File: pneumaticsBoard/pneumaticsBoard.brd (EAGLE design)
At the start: 188 x 25.4 mm, 52 parts, among them IC1 MAX232, Q1 BSS296, Q2 BSS296, Q3 BSS296, Q4 BSS296, Q5 BSS296, Q6 BSS296, Q7 BSS296, Q8 BSS296, U1 ATMEGA328P-PU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

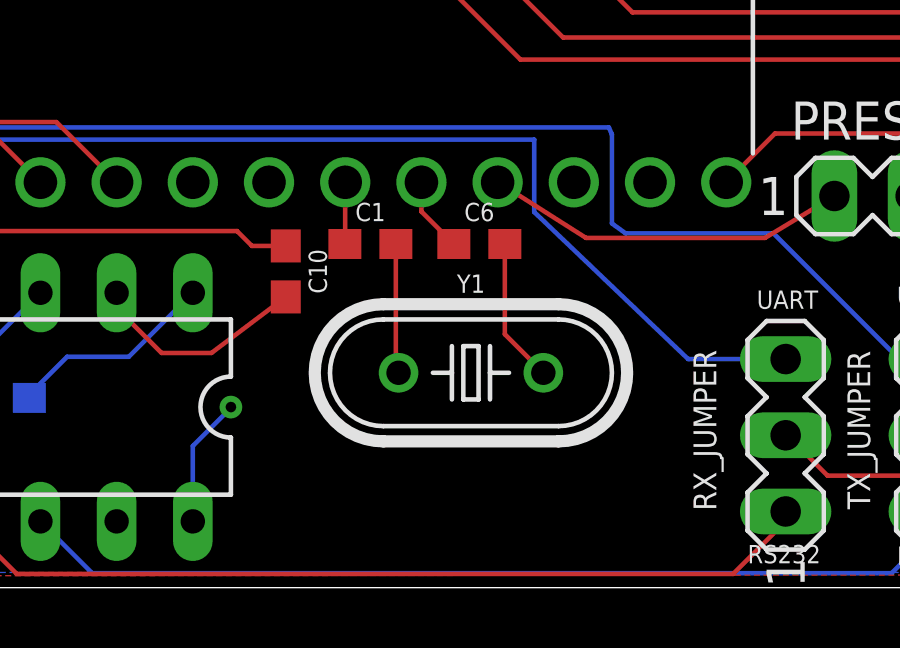
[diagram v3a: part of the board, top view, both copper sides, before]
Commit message: Crystal Circuit wasn't grounded
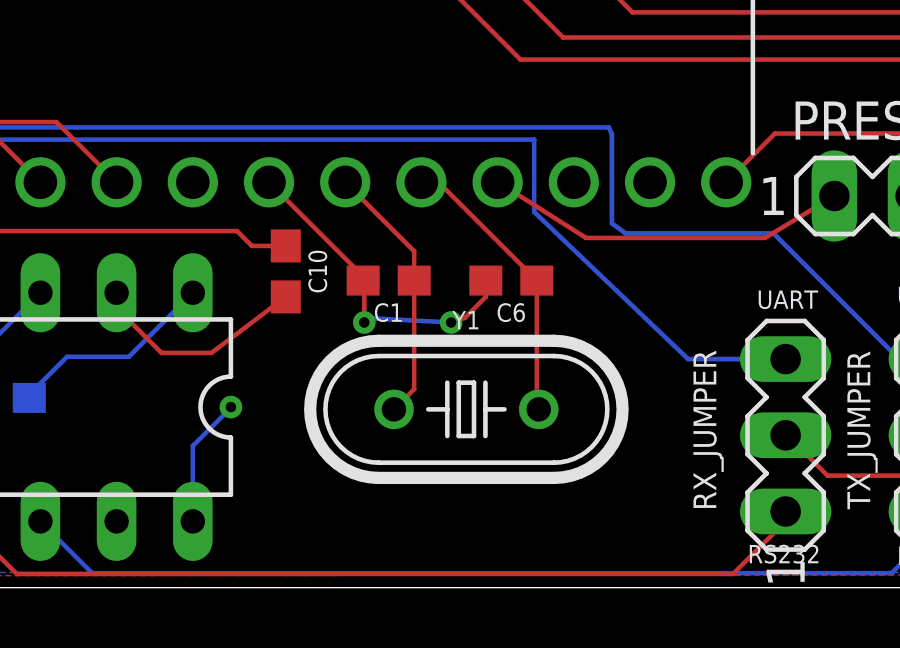
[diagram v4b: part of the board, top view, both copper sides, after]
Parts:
- moved C6 1.62 mm to (48.6, 10.2), turned to 180 degrees
- moved C1 1.36 mm to (44.6, 10.2), turned to 180 degrees
- moved Y1 1.23 mm to (47.1, 5.94)
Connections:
- removed net N$15: C1.2, Y1.1
- removed net N$5: C6.2, Y1.2
- net GND: now also C1.2, C6.2
- net XTAL1: now also Y1.1
- net XTAL2: now also Y1.2
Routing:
- net GND: track 33.7 -> 44.8 mm, vias 0 -> 2
- net XTAL2: track 2.50 -> 9.52 mm
- net XTAL1: track 2.06 -> 8.80 mm
- net N$5: track 4.82 -> 0.00 mm
- net N$15: track 4.33 -> 0.00 mm
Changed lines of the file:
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@@
 <attribute name="SUPPLIER" value="Atmel" x="55.8038" y="21.1328" size="1.778" layer="27" rot="R90" display="off"/>
 </element>
-<element name="Y1" library="SparkFun-Clocks" package="HC49U" value="16 MHz" x="47.2948" y="7.1628"/>
+<element name="Y1" library="SparkFun-Clocks" package="HC49U" value="16 MHz" x="47.1424" y="5.9436"/>
 <element name="CON1" library="pinhead" package="1X02" value="" x="178.7398" y="3.9878"/>
 <element name="CON2" library="pinhead" package="1X02" value="" x="168.5798" y="3.9878"/>
@@
 <attribute name="VALUE" x="76.1492" y="14.097" size="1.27" layer="27" ratio="10" rot="R180"/>
 </element>
-<element name="C6" library="SparkFun-Capacitors" package="0603" value="22pF" x="47.5742" y="11.4554">
-<attribute name="PROD_ID" value="CAP-07884" x="47.5742" y="11.4554" size="1.778" layer="27" display="off"/>
+<element name="C6" library="SparkFun-Capacitors" package="0603" value="22pF" x="48.641" y="10.2362" rot="R180">
+<attribute name="PROD_ID" value="CAP-07884" x="48.641" y="10.2362" size="1.778" layer="27" rot="R180" display="off"/>
 </element>
 <element name="C8" library="SparkFun-Capacitors" package="0603" value="1uF" x="31.7246" y="6.3246" rot="MR0">
@@
 <attribute name="PROD_ID" value="CAP-07884" x="41.1226" y="10.541" size="1.778" layer="27" rot="R270" display="off"/>
 </element>
-<element name="C1" library="SparkFun-Capacitors" package="0603" value="22pF" x="43.942" y="11.4554">
-<attribute name="PROD_ID" value="CAP-07884" x="43.942" y="11.4554" size="1.778" layer="27" display="off"/>
+<element name="C1" library="SparkFun-Capacitors" package="0603" value="22pF" x="44.5516" y="10.2362" rot="R180">
+<attribute name="PROD_ID" value="CAP-07884" x="44.5516" y="10.2362" size="1.778" layer="27" rot="R180" display="off"/>
 </element>
 <element name="PRESSURE" library="con-lstb" library_urn="urn:adsk.eagle:library:162" package="MA03-1" package3d_urn="urn:adsk.eagle:package:8339/1" value="" x="61.9506" y="13.0556" smashed="yes">
@@
 <signal name="XTAL1">
 <contactref element="U1" pad="9"/>
+<contactref element="Y1" pad="1"/>
 <contactref element="C1" pad="1"/>
-<wire x1="43.1038" y1="13.5128" x2="43.1038" y2="11.4672" width="0.1524" layer="1"/>
-<wire x1="43.1038" y1="11.4672" x2="43.092" y2="11.4554" width="0.1524" layer="1"/>
+<wire x1="45.4016" y1="6.6158" x2="45.4016" y2="10.2362" width="0.1524" layer="1"/>
+<wire x1="45.4016" y1="6.6158" x2="44.7294" y2="5.9436" width="0.1524" layer="1"/>
+<wire x1="45.4016" y1="10.2362" x2="45.4016" y2="11.215" width="0.1524" layer="1"/>
+<wire x1="45.4016" y1="11.215" x2="43.1038" y2="13.5128" width="0.1524" layer="1"/>
 </signal>
 <signal name="XTAL2">
 <contactref element="U1" pad="10"/>
 <contactref element="C6" pad="1"/>
-<wire x1="45.6438" y1="13.5128" x2="45.6438" y2="12.5358" width="0.1524" layer="1"/>
-<wire x1="45.6438" y1="12.5358" x2="46.7242" y2="11.4554" width="0.1524" layer="1"/>
+<contactref element="Y1" pad="2"/>
+<wire x1="49.491" y1="10.2362" x2="49.491" y2="6.008" width="0.1524" layer="1"/>
+<wire x1="49.491" y1="6.008" x2="49.5554" y2="5.9436" width="0.1524" layer="1"/>
+<wire x1="45.6438" y1="13.5128" x2="46.2144" y2="13.5128" width="0.1524" layer="1"/>
+<wire x1="46.2144" y1="13.5128" x2="49.491" y2="10.2362" width="0.1524" layer="1"/>
 </signal>
 <signal name="Q8">
@@
 <contactref element="Q7" pad="3"/>
 <contactref element="Q1" pad="3"/>
+<contactref element="C6" pad="2"/>
+<contactref element="C1" pad="2"/>
+<wire x1="47.791" y1="10.2362" x2="47.791" y2="9.691" width="0.1524" layer="1"/>
+<wire x1="47.791" y1="9.691" x2="47.0916" y2="8.9916" width="0.1524" layer="1"/>
+<wire x1="47.0916" y1="8.9916" x2="46.6344" y2="8.8392" width="0.1524" layer="1"/>
+<via x="46.6344" y="8.8392" extent="1-16" drill="0.35"/>
+<wire x1="46.6344" y1="8.8392" x2="43.7388" y2="8.9916" width="0.1524" layer="16"/>
+<wire x1="43.7388" y1="8.9916" x2="43.7388" y2="8.8392" width="0.1524" layer="16"/>
+<via x="43.7388" y="8.8392" extent="1-16" drill="0.35"/>
+<wire x1="43.7388" y1="8.8392" x2="43.7388" y2="10.199" width="0.1524" layer="1"/>
+<wire x1="43.7388" y1="10.199" x2="43.7016" y2="10.2362" width="0.1524" layer="1"/>
+<wire x1="43.7016" y1="10.2362" x2="43.7016" y2="10.375" width="0.1524" layer="1"/>
+<wire x1="43.7016" y1="10.375" x2="40.5638" y2="13.5128" width="0.1524" layer="1"/>
 </signal>
 <signal name="VDD">
@@
 <wire x1="27.686" y1="15.875" x2="32.9438" y2="21.1328" width="0.1524" layer="1"/>
 </signal>
-<signal name="N$5">
-<contactref element="C6" pad="2"/>
-<contactref element="Y1" pad="2"/>
-<wire x1="48.4242" y1="11.4554" x2="48.4242" y2="8.4464" width="0.1524" layer="1"/>
-<wire x1="48.4242" y1="8.4464" x2="49.7078" y2="7.1628" width="0.1524" layer="1"/>
-</signal>
-<signal name="N$15">
-<contactref element="Y1" pad="1"/>
-<contactref element="C1" pad="2"/>
-<wire x1="44.792" y1="11.4554" x2="44.792" y2="7.2526" width="0.1524" layer="1"/>
-<wire x1="44.792" y1="7.2526" x2="44.8818" y2="7.1628" width="0.1524" layer="1"/>
-</signal>
 <signal name="N$6">

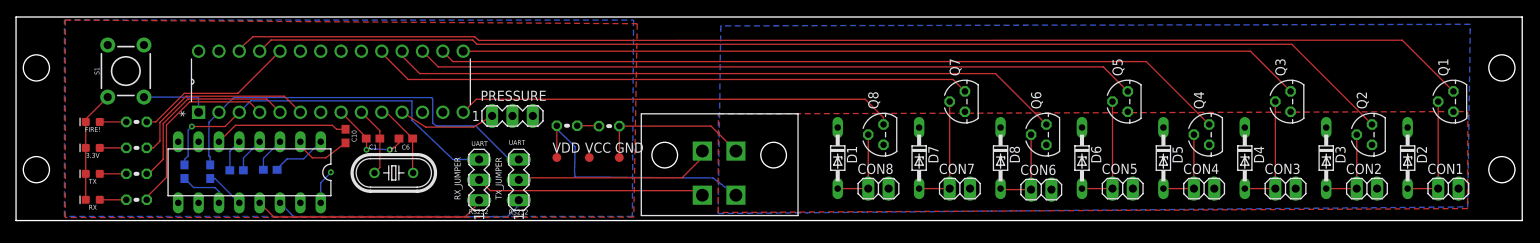
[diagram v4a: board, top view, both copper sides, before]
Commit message: PN - changed VD to Reg, added pressure sensor, added silkscreen to proper layer
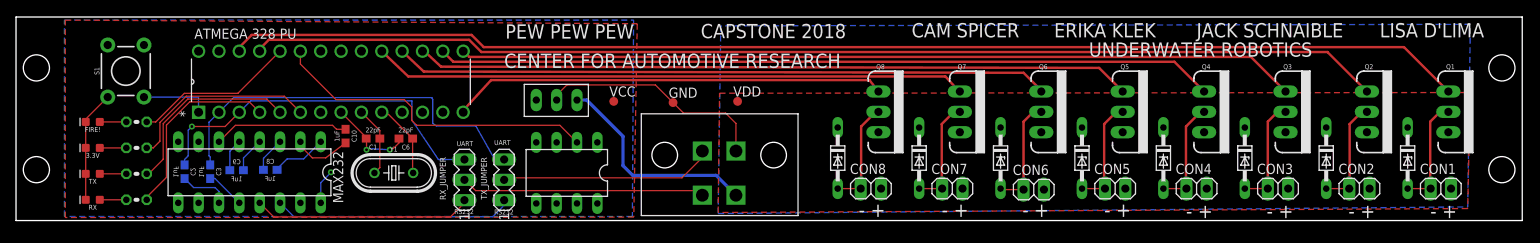
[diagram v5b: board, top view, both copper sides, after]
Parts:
- removed PRESSURE: (no value), con-lstb:MA03-1
- removed R4: 4.7 K, resistor:0204V
- removed R6: 3.3 K, resistor:0204V
- added PRESSURE_SENSOR: (no value), ic-package:DIL08
- added U$1: L78M05CV, L78M05CV:L78M05CV
- Q1, Q2, Q3, Q4, Q5, Q6, Q7, Q8: value BSS296 -> 60V/32A/35mΩ; device transistor-fet:TO92 -> SparkFun-DiscreteSemi:TO220V
- moved VDD 23.6 mm to (90.0, 14.9)
- moved GND 9.59 mm to (82.0, 14.7)
- moved VCC 7.64 mm to (74.6, 14.9)
- moved Q6 2.91 mm to (127.9, 13.6), turned to 270 degrees
- moved Q8 2.91 mm to (107.6, 13.6), turned to 270 degrees
- moved Q2 2.91 mm to (168.6, 13.6), turned to 270 degrees
- moved Q4 2.91 mm to (148.3, 13.6), turned to 270 degrees
- moved TX_JUMPER 1.83 mm to (60.9, 5.08)
- moved RX_JUMPER 1.83 mm to (56.0, 5.08)
- moved Q5 1.43 mm to (138.1, 13.6), turned to 270 degrees
- moved Q7 1.43 mm to (117.8, 13.6), turned to 270 degrees
- moved Q1 1.43 mm to (178.7, 13.6), turned to 270 degrees
- moved Q3 1.43 mm to (158.4, 13.6), turned to 270 degrees
- moved CON2 0.94 mm to (167.6, 3.99)
- moved CON3 0.94 mm to (157.5, 3.99)
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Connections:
- removed net N$6: PRESSURE.1, U1.11
- new net PRESSURE: PRESSURE_SENSOR.2, U1.23
- net GND: now also PRESSURE_SENSOR.3, U$1.GROUND; no longer PRESSURE.3, R6.1
- net VCC: now also PRESSURE_SENSOR.1, U$1.OUTPUT; no longer PRESSURE.2, R4.1, R6.2
- net VDD: now also U$1.INPUT; no longer R4.2
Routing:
- net PRESSURE: track 0.00 -> 41.2 mm
- net N$6: track 12.2 -> 0.00 mm
- net GND: track 44.8 -> 54.1 mm
- net VDD: track 32.5 -> 26.9 mm
- net CON6_GND: track 10.7 -> 14.2 mm
- net CON2_GND: track 10.5 -> 13.8 mm
- net CON8_GND: track 10.5 -> 13.7 mm
- net CON4_GND: track 10.5 -> 13.6 mm
- net VCC: track 7.05 -> 4.31 mm
- net Q6: track 84.5 -> 81.8 mm
- net Q4: track 99.4 -> 97.1 mm
- net Q2: track 143.8 -> 141.6 mm
- net TX_ORIGINAL: track 24.9 -> 26.7 mm
- net N$3: track 31.7 -> 29.9 mm
- net RX_ORIGINAL: track 28.7 -> 30.5 mm
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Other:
- board text added: "- +"
- board text removed: "WEAPONS INITIATION SYSTEM"

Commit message: Changed regulator position, fixed traces
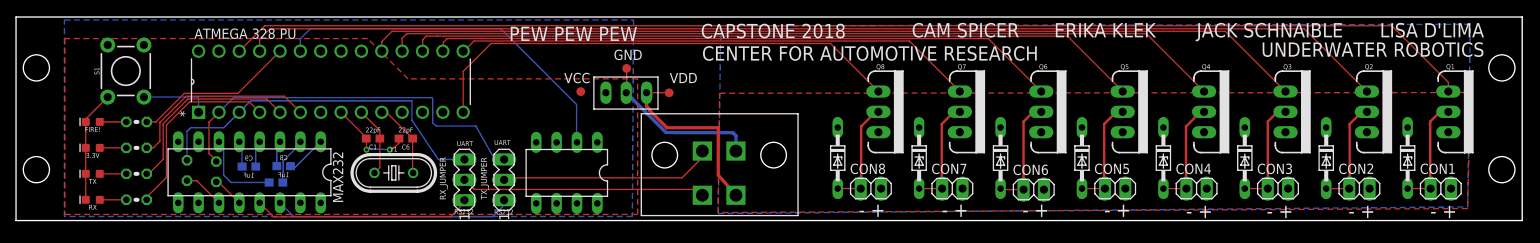
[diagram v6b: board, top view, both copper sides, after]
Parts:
- removed C2, C3: 1uF, SparkFun-Capacitors:0603
- added SW1, SW2: (no value), resistor:0204V
- moved C10 10.4 mm to (32.4, 4.75), flipped to the bottom, turned to 180 degrees
- moved U$1 8.73 mm to (73.6, 13.4)
- moved VDD 8.60 mm to (81.5, 15.9)
- moved GND 7.19 mm to (76.2, 19.0)
- moved VCC 4.29 mm to (70.5, 16.1)
- moved C8 1.74 mm to (33.4, 6.78)
- moved C9 1.59 mm to (29.1, 6.73)
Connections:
- removed net Q4: Q4.1, U1.16
- new net N$5: Q4.1, U1.18
- net N$17: now also SW1.1; no longer C2.1
- net N$18: now also SW2.1; no longer C3.1
- net Q3: now also U1.19; no longer U1.15
- net Q6: now also U1.16; no longer U1.18
- net Q7: now also U1.15; no longer U1.19
- net RX: now also SW2.2; no longer C3.2
- net TX: now also SW1.2; no longer C2.2
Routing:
- net N$5: track 0.00 -> 104.9 mm
- net Q4: track 97.1 -> 0.00 mm
- net Q3: track 104.7 -> 117.6 mm
- net Q7: track 74.2 -> 65.1 mm
- net GND: track 54.1 -> 45.9 mm
- net Q8: track 54.4 -> 60.8 mm
- net N$14: track 16.9 -> 10.5 mm
- net VCC: track 4.31 -> 0.00 mm, vias 1 -> 0
- net PRESSURE: track 41.2 -> 45.2 mm
- net Q6: track 81.8 -> 78.6 mm
- net VDD: track 26.9 -> 23.9 mm
- net Q5: track 89.4 -> 91.8 mm
- net Q2: track 141.6 -> 143.5 mm
- net N$9: track 6.97 -> 5.12 mm
- net N$13: track 7.39 -> 5.99 mm
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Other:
- board text added: "GND"
- board text added: "RX"
- board text added: "TX"
- board text added: "VDD"
